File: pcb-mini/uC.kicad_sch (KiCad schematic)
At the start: 33 parts, among them SW7 SW_Push, U2 RP2350_80QFN, U6 W25Q128JVS, Y2 ABM8-272-T3

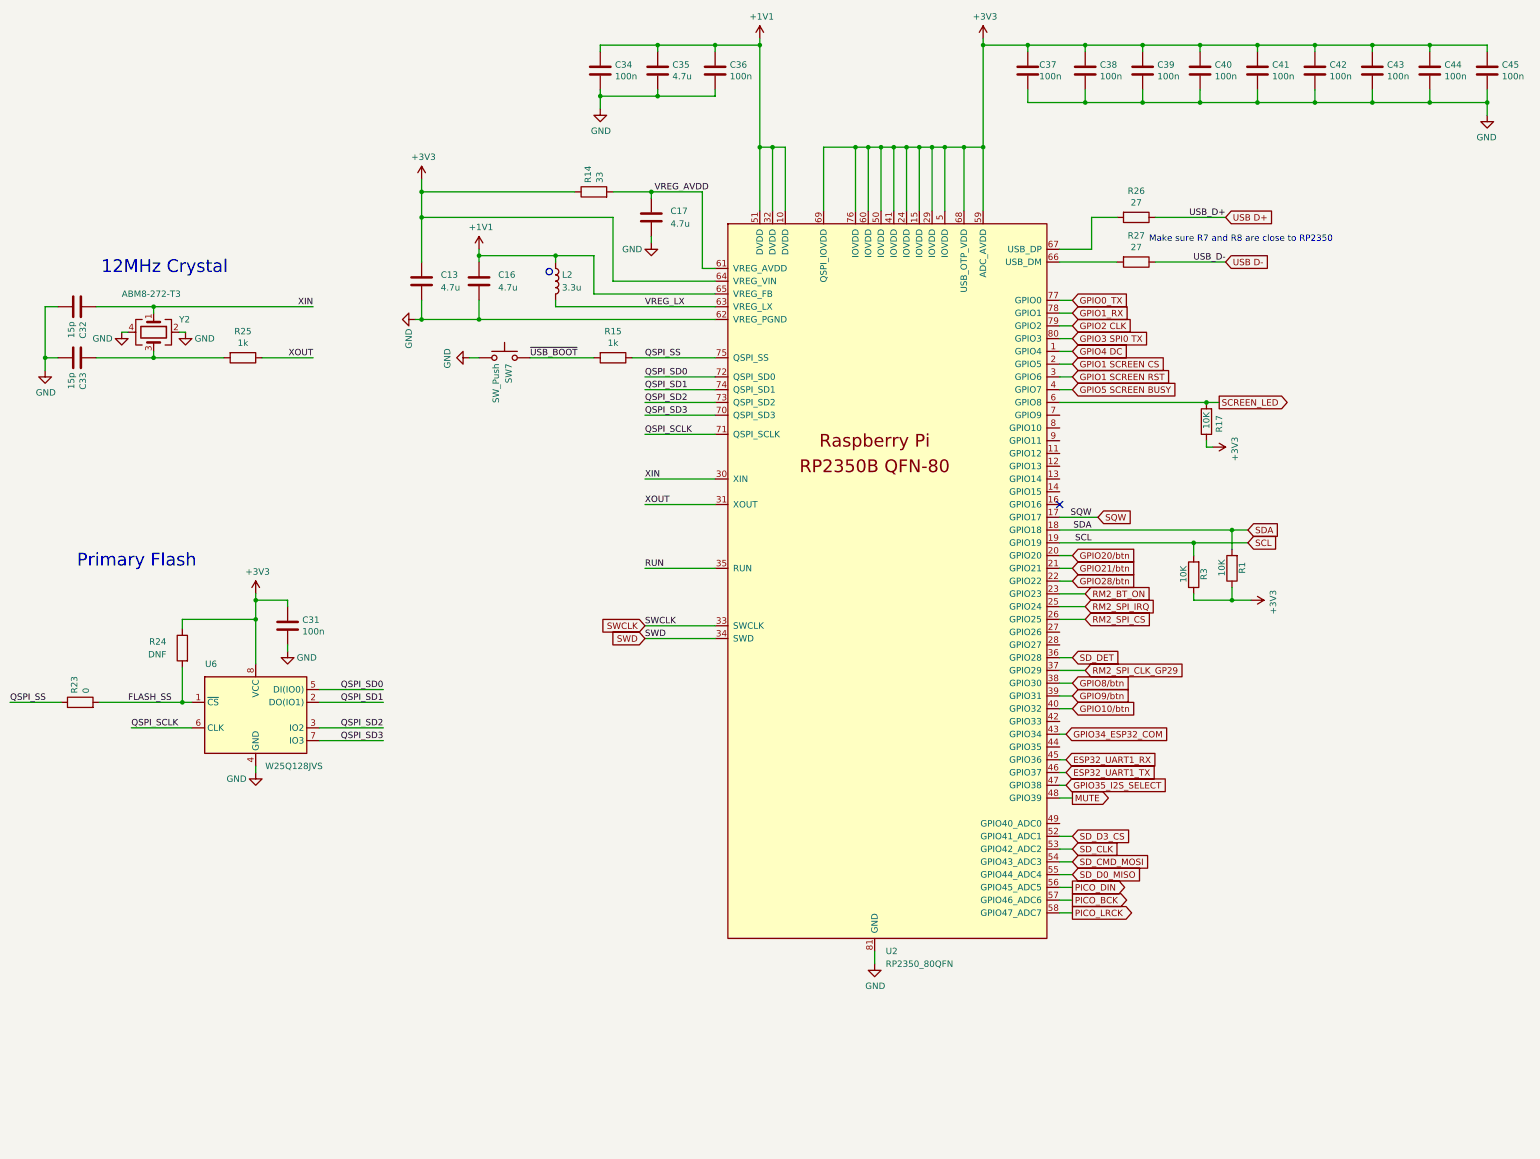
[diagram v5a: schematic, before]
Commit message: [pcb] mini: add/fix LCSC refs
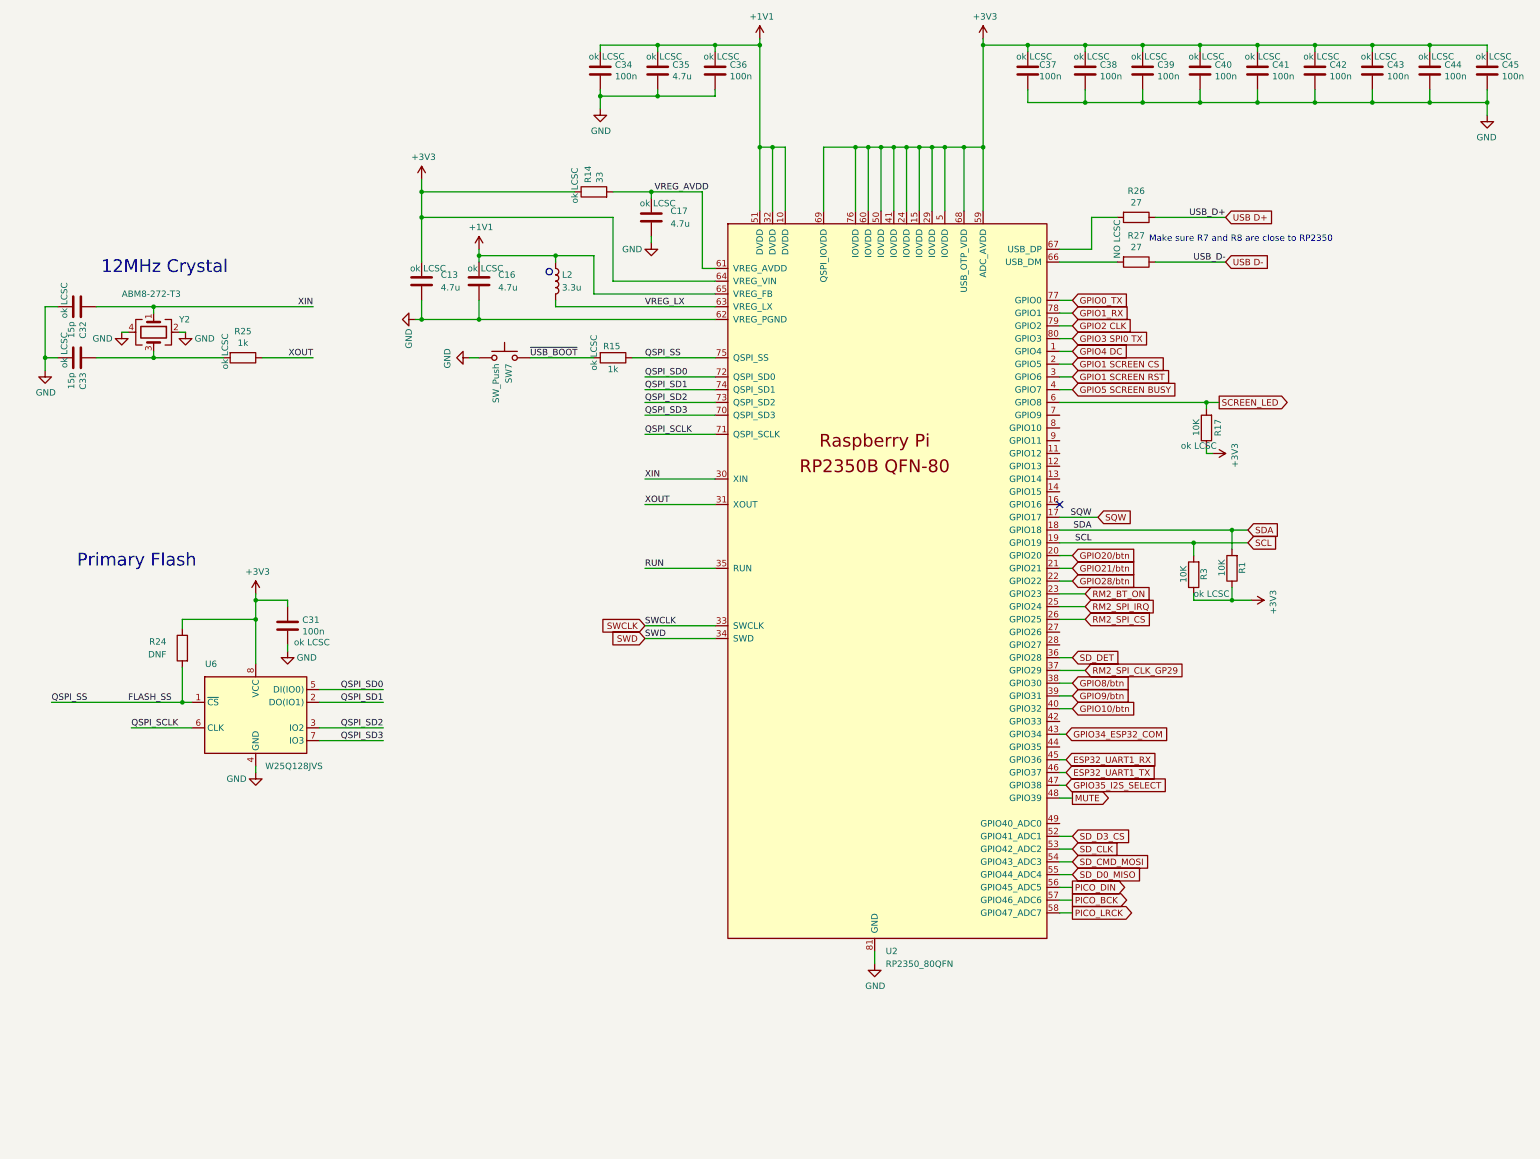
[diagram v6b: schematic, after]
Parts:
- removed R23: 0, Resistor_SMD:R_0402_1005Metric, symbol Device:R
- C13, C16, C17, C35: LCSC (none) -> C23733
- C31, C34, C36, C37, C38, C39, C40, C41, C42, C43, C44, C45: LCSC (none) -> C1525
- C32, C33: LCSC (none) -> C1548
- R1, R17, R3: footprint Resistor_SMD:R_0603_1608Metric -> Resistor_SMD:R_0402_1005Metric
- R14: LCSC (none) -> C25105
- R15, R25: LCSC (none) -> C11702
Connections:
- net QSPI_SS is gone; now on net FLASH_SS: R15.1, U2.75 (QSPI_SS)
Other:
- moved on the sheet: R17

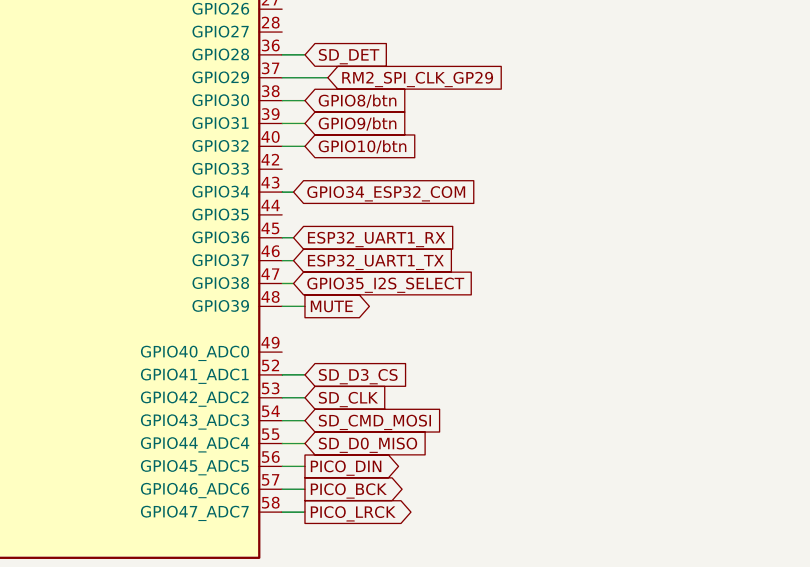
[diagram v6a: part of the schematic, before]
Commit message: [pcb] mini: fix audio connector, resistor on 74LS157
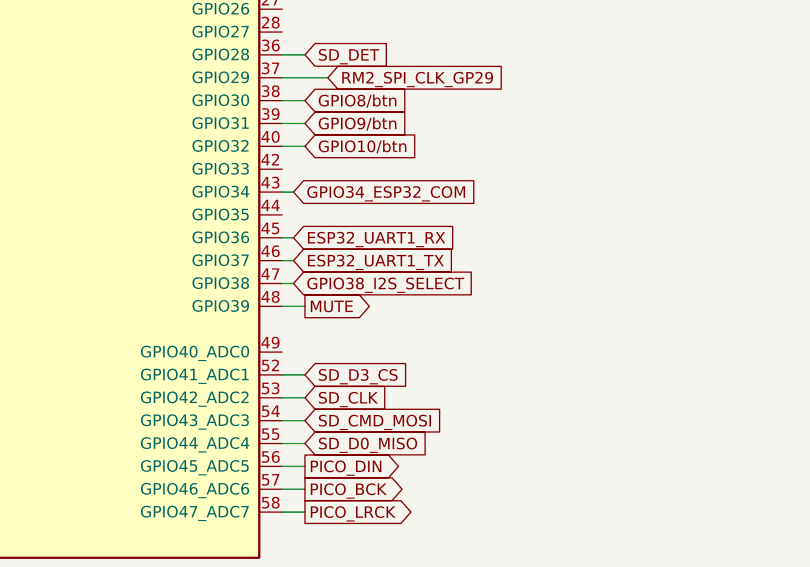
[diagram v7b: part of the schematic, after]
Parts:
- L2: LCSC (none) -> C42411119
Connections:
- net GPIO35_I2S_SELECT renamed GPIO38_I2S_SELECT
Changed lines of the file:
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@@
 		)
 	)
-	(global_label "GPIO35_I2S_SELECT"
+	(global_label "GPIO38_I2S_SELECT"
 		(shape input)
 		(at 243.84 204.47 0)
@@
 			)
 		)
+		(property "LCSC" "C42411119"
+			(at 142.24 104.14 0)
+			(effects
+				(font
+					(size 1.27 1.27)
+				)
+				(hide yes)
+			)
+		)

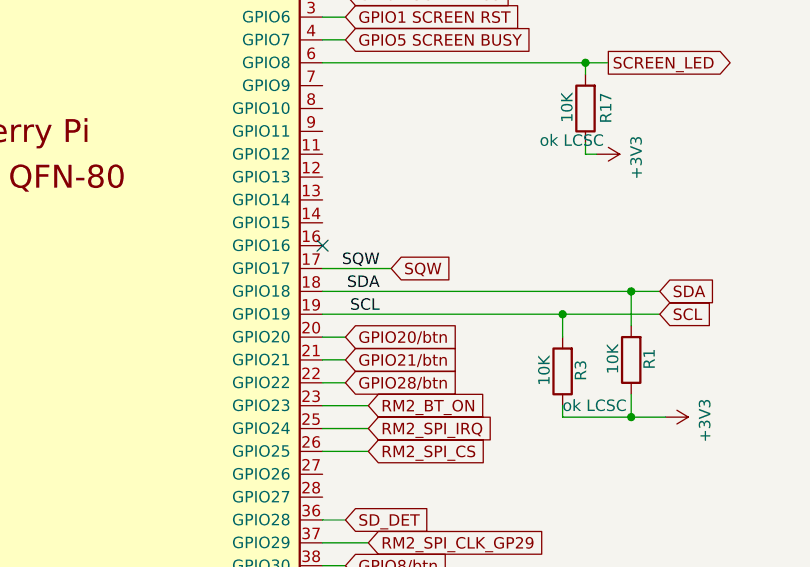
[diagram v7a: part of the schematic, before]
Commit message: [pcb] mini: RTC: add diods, wire INT. fix 74LS chip footprint
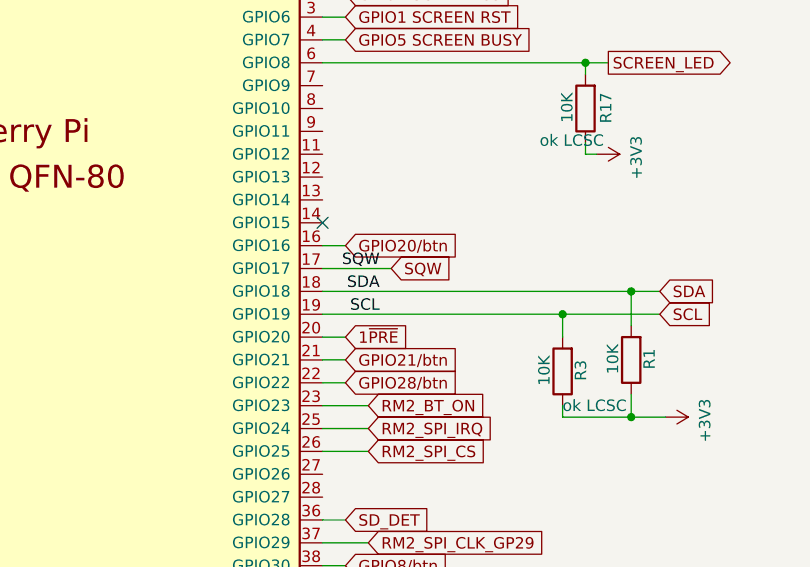
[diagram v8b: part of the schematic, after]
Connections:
- net GPIO20/btn: now also U2.16 (GPIO16); no longer U2.20 (GPIO20)
- new net 1~{PRE}: U2.20 (GPIO20)
